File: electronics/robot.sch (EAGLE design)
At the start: 77 parts, among them J1 USB-B, J2 DC21MMX, J3 B6B-ZR, J4 B6B-ZR, J5 B6B-ZR, J6 KICKER, Q1 IRLMS2002TRPBF, Q2 IRLMS2002TRPBF, Q3 NPN_BC817,215, Q4 SUD50N04-8M8P-4GE3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

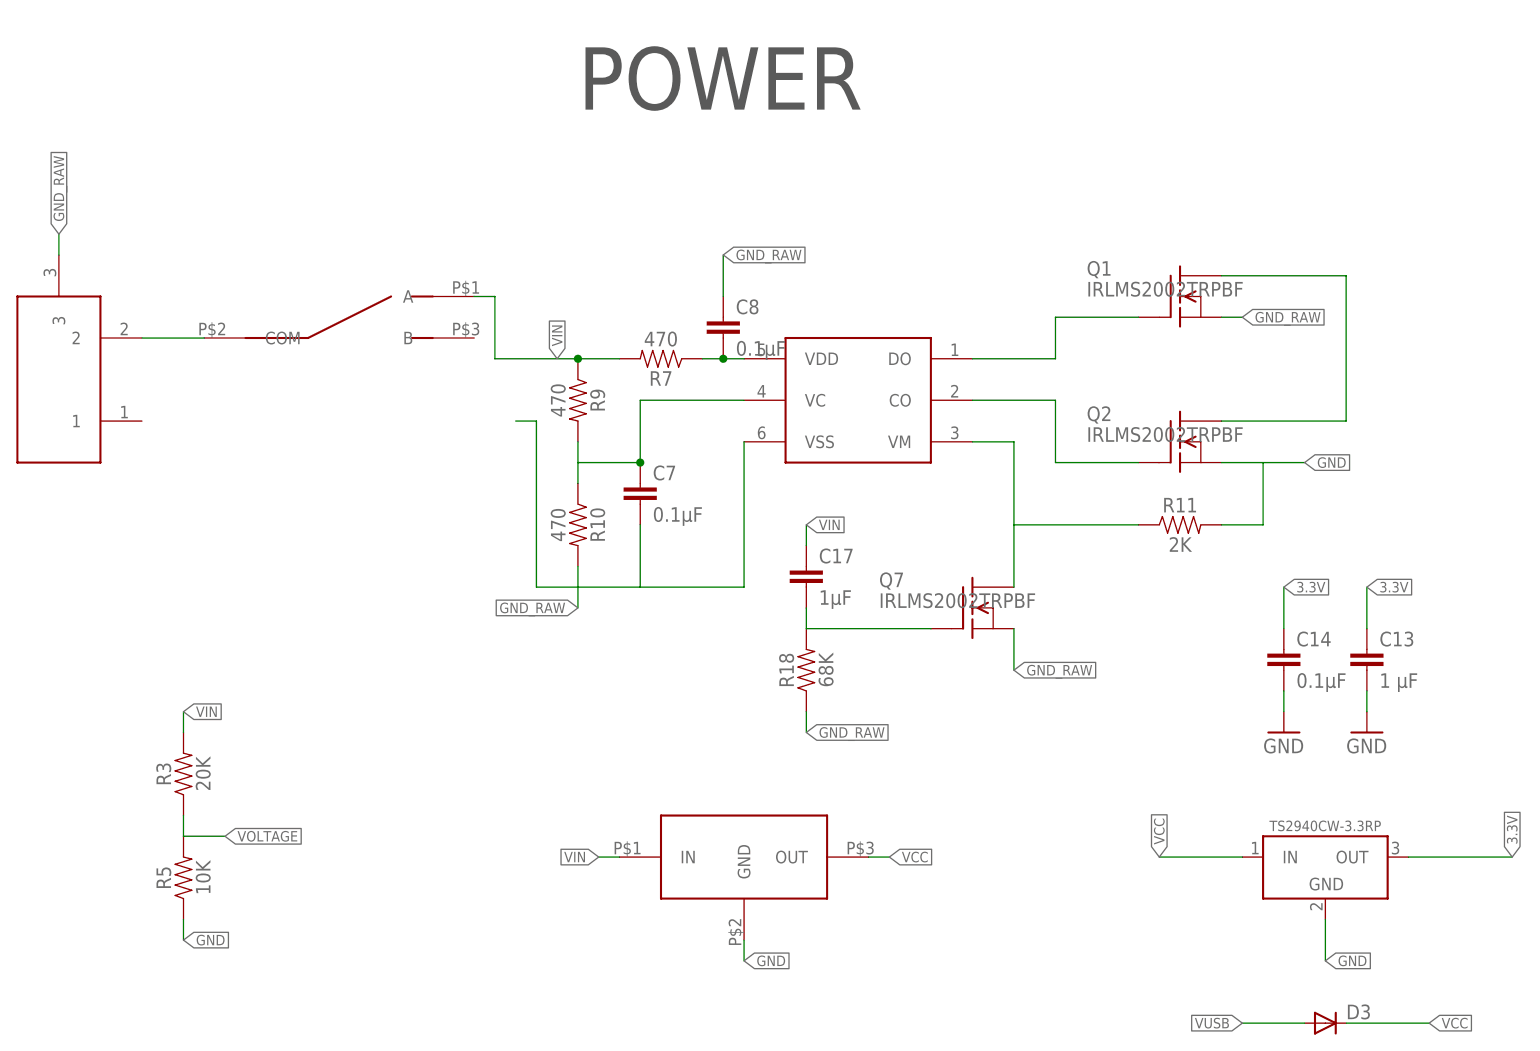
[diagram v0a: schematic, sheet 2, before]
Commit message: Adding D2 diode
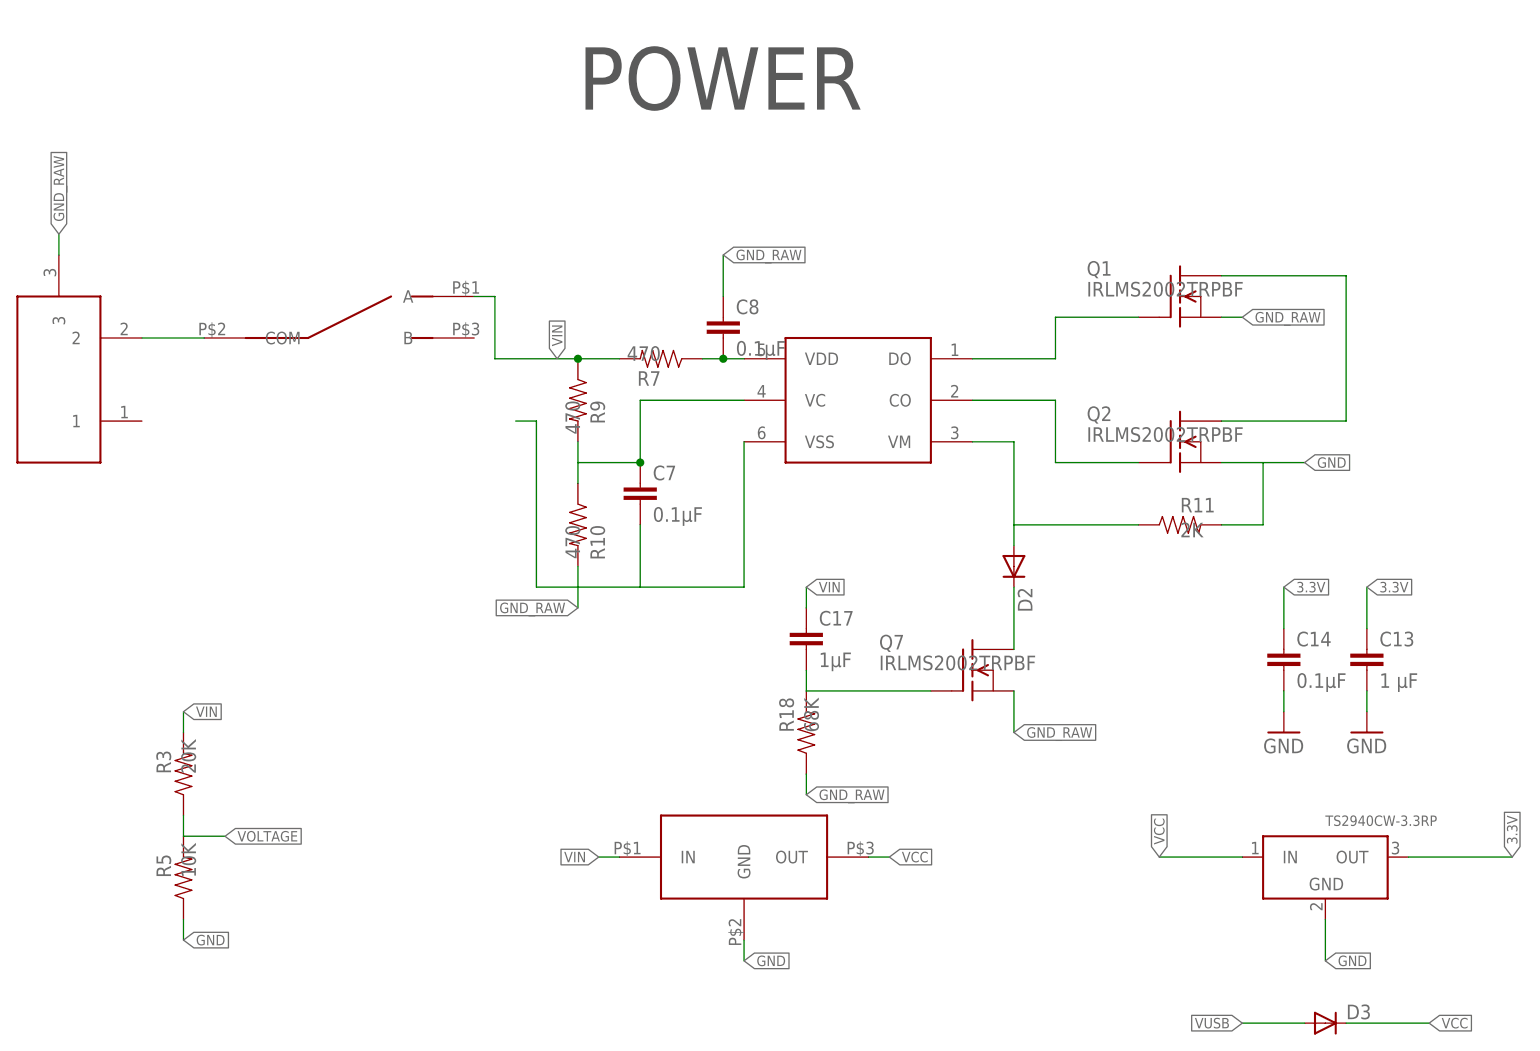
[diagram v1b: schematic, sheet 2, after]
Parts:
- added D2: (no value), SparkFun-DiscreteSemi:DIODESOD
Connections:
- new net N$22: D2.C, Q7.D
- net N$13: now also D2.A; no longer Q7.D
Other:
- moved on the sheet: C17, Q7, R18

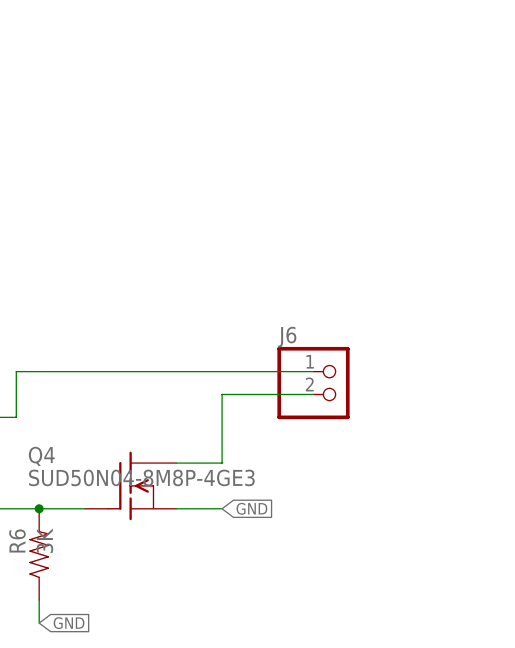
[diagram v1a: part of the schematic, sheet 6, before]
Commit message: Adding RS1M footprint (wip)
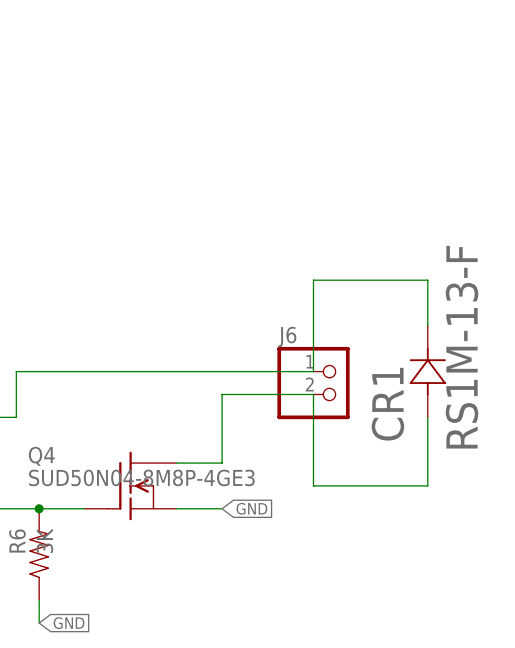
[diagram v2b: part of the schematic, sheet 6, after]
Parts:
- added CR1: RS1M-13-F, custom:RS1M-13-F
- J6: value KICKER -> RHOBAN_KICKER; device rhoban:KICKER -> robot:RHOBAN_KICKER
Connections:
- net KICKER: now also CR1.A
- net VSTORE: now also CR1.K
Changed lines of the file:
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@@
 <attribute name="FARNELL" value="1146032"/>
 </part>
-<part name="J6" library="rhoban" deviceset="KICKER" device="">
+<part name="J6" library="robot" deviceset="RHOBAN_KICKER" device="">
 <attribute name="FARNELL" value="JF-0530B"/>
 </part>
@@
 <attribute name="FARNELL" value="8737843RL"/>
 </part>
+<part name="CR1" library="custom" deviceset="RS1M-13-F" device=""/>
 </parts>
 <sheets>
@@
 <attribute name="VALUE" x="43.942" y="-8.89" size="1.778" layer="96" rot="R90"/>
 </instance>
+<instance part="CR1" gate="A" x="119.38" y="-12.7" rot="R90"/>
 </instances>
 <busses>
@@
 <pinref part="C20" gate="G$1" pin="+"/>
 <pinref part="R14" gate="G$1" pin="1"/>
+<pinref part="CR1" gate="A" pin="K"/>
+<wire x1="119.38" y1="-2.54" x2="119.38" y2="2.54" width="0.1524" layer="91"/>
+<wire x1="119.38" y1="2.54" x2="106.68" y2="2.54" width="0.1524" layer="91"/>
+<wire x1="106.68" y1="2.54" x2="106.68" y2="-7.62" width="0.1524" layer="91"/>
 </segment>
 </net>
@@
 <wire x1="96.52" y1="-10.16" x2="106.68" y2="-10.16" width="0.1524" layer="91"/>
 <pinref part="J6" gate="A" pin="2"/>
-</segment>
-</net>
+<pinref part="CR1" gate="A" pin="A"/>
+<wire x1="119.38" y1="-12.7" x2="119.38" y2="-20.32" width="0.1524" layer="91"/>
+<wire x1="119.38" y1="-20.32" x2="106.68" y2="-20.32" width="0.1524" layer="91"/>
+<wire x1="106.68" y1="-20.32" x2="106.68" y2="-10.16" width="0.1524" layer="91"/>
+</segment>
+</net>
